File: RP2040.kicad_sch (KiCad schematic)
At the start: 36 parts, among them J301 Conn_01x03, SW1 BOOT, SW2 RUN, U3 RP2040, U5 W25Q128JVPIQ, Y301 12.000 MHz

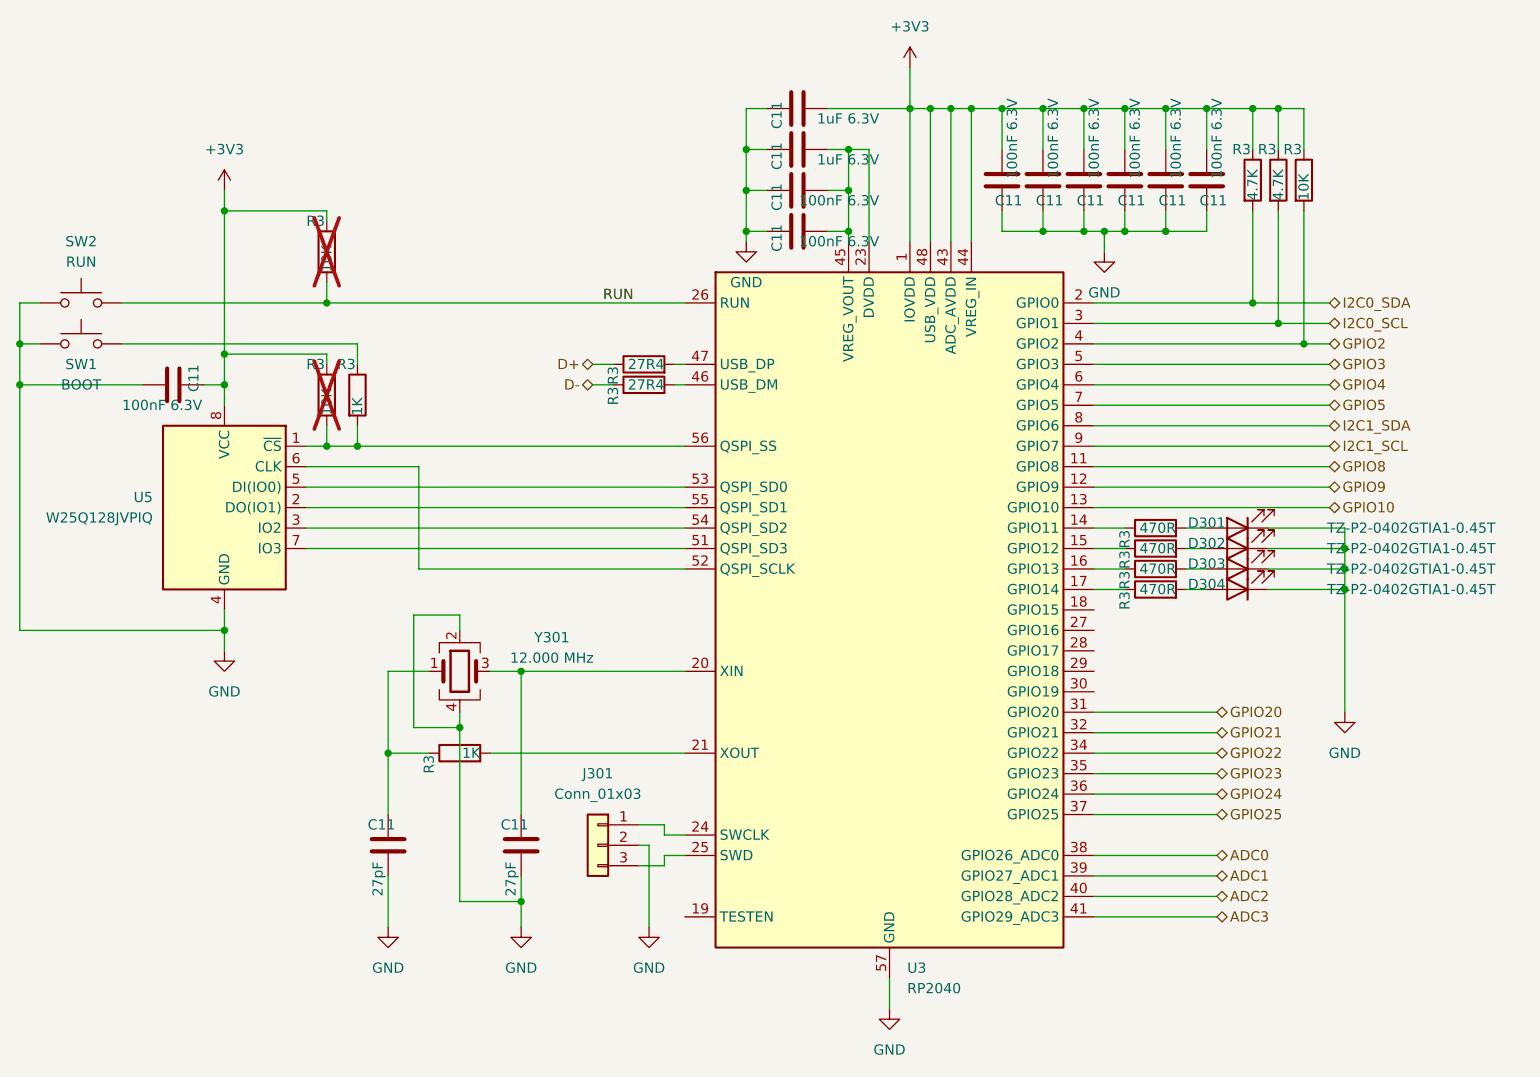
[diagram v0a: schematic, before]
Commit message: Create PDF's of design.
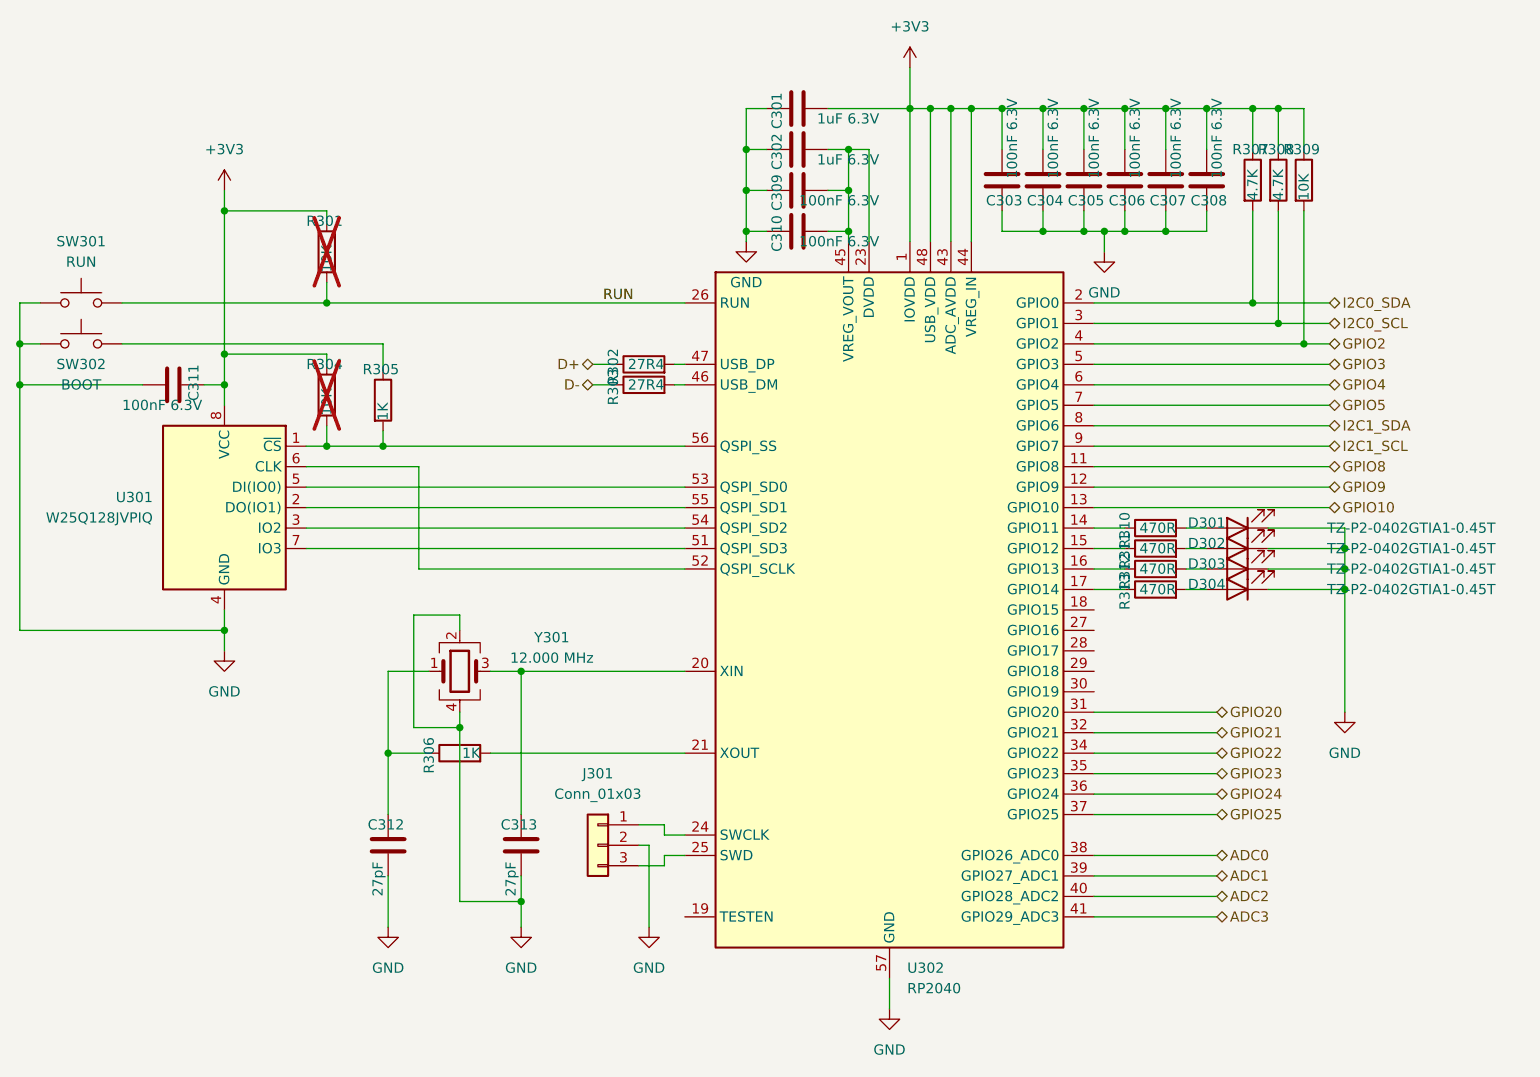
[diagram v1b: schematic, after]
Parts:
- renumbered C11 to C301, C11 to C302, C11 to C303, C11 to C304, C11 to C305, C11 to C306, C11 to C307, C11 to C308, C11 to C309, C11 to C310, C11 to C311, C11 to C312, C11 to C313, R3 to R301, R3 to R302, R3 to R303, R3 to R304, R3 to R305, R3 to R306, R3 to R307, R3 to R308, R3 to R309, R3 to R310, R3 to R311, R3 to R312, R3 to R313, SW2 to SW301, SW1 to SW302, U5 to U301, U3 to U302
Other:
- moved on the sheet: R305
